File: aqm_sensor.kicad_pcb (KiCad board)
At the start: 2 copper layers, 45 x 30 mm, 14 parts, among them J2 QWIIC, J3 PMS5003, U3 ESP32-C3_SUPERMINI_TH

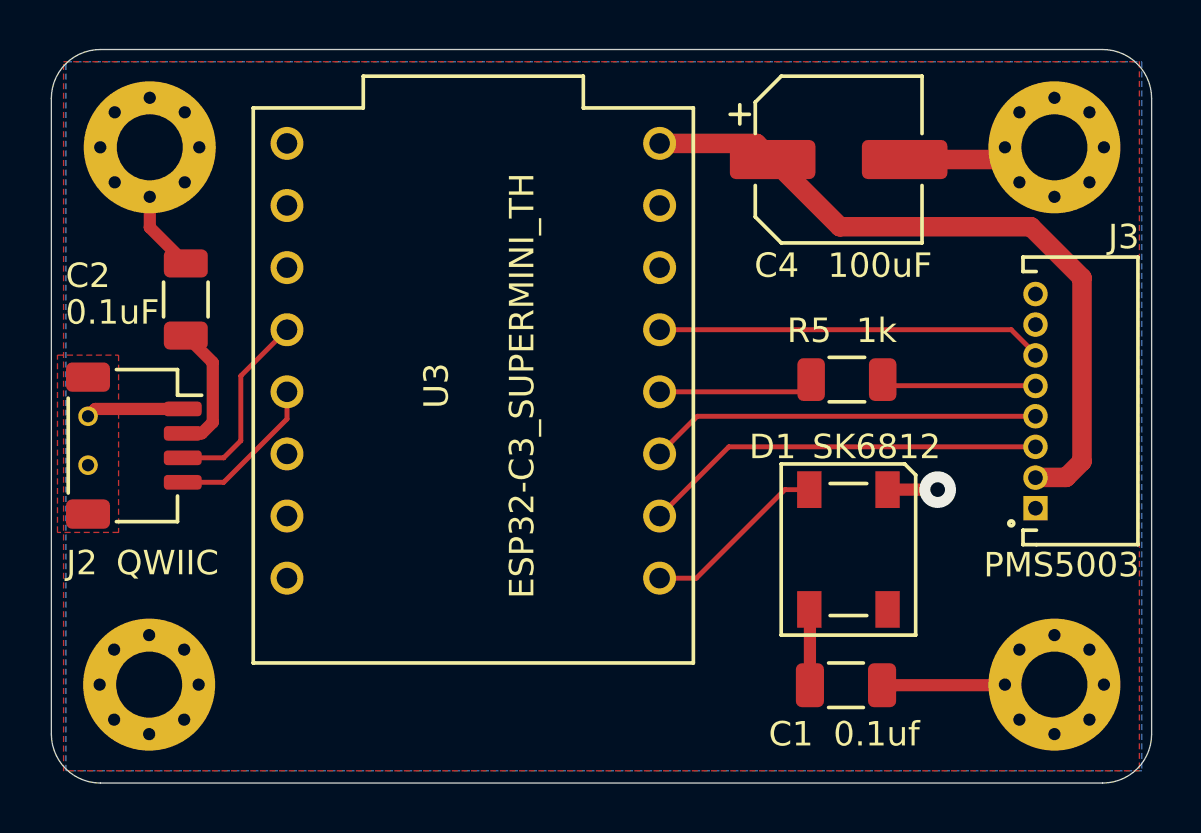
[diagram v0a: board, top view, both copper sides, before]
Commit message: v2 schematic and PCB rework
Schematic:
- Rewire J3 for PMS5003 cable mirror (pin 1↔8 reversal)
- Add I2C pull-up resistors R1, R2 (4.7k) on SDA/SCL
- Replace C4 100uF electrolytic with 10uF 0805 ceramic
- Fix J3 pin types from Unspecified to Passive (ERC clean)
- Add test points: TP1/TP2 (loop) for RX/TX, TP3-TP5 (pad) for power
- Fix C1 value capitalization (0.1uf → 0.1uF)

PCB:
- Rotate U3 180° to correct antenna orientation
- Place new components (R1, R2, C4, TP1-TP5)
- Reroute for updated netlist
- Add GND stitching vias

Removes TODO.md (tracked in CLAUDE.md known issues).

Co-Authored-By: Claude Opus 4.6 (1M context) <noreply@anthropic.com>
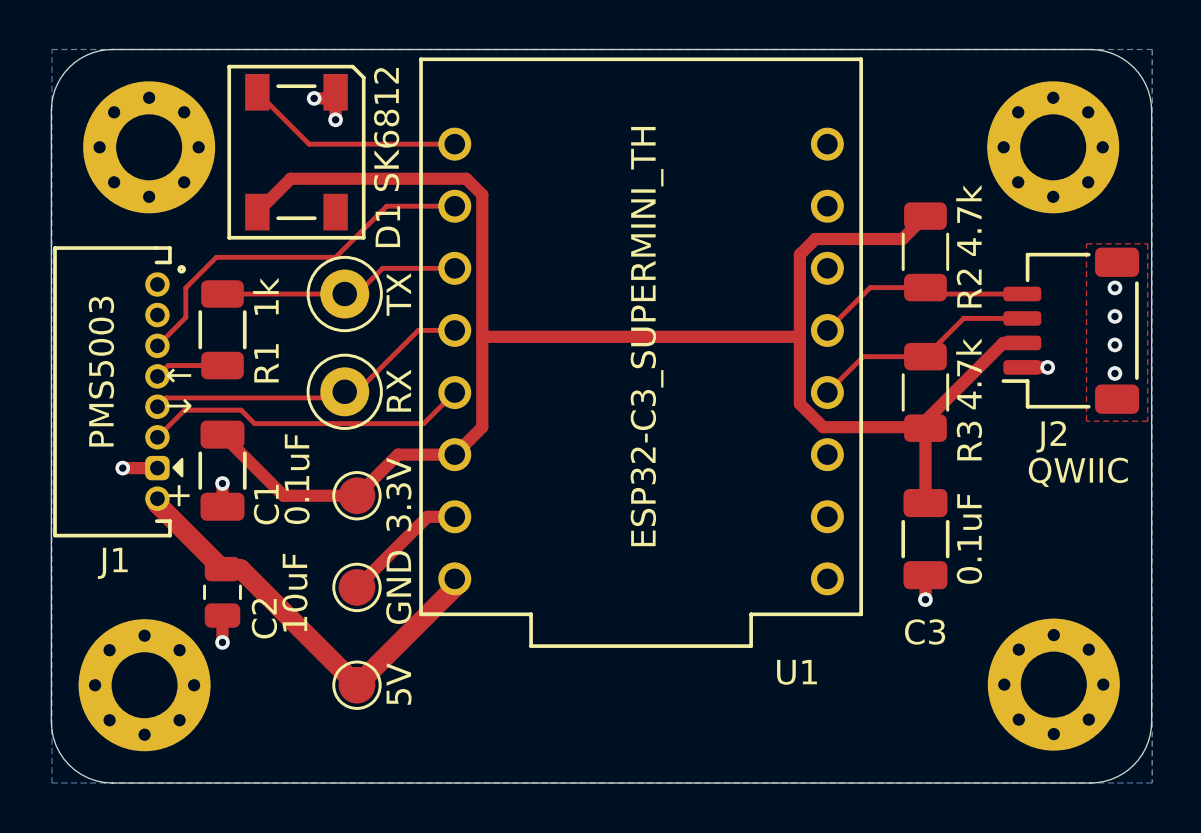
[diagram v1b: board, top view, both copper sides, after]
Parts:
- removed ? (x2): , 
- added R2: 4.7k, Resistor_SMD:R_1206_3216Metric, F.Cu at (181.3, 78.9)
- added R3: 4.7k, Resistor_SMD:R_1206_3216Metric, F.Cu at (181.3, 84.6)
- added TP1: TX, TestPoint:TestPoint_Loop_D2.50mm_Drill1.0mm, F.Cu at (157.6, 80.6)
- added TP2: 3.3V, TestPoint:TestPoint_Pad_D1.5mm, F.Cu at (158.1, 88.8)
- added TP3: RX, TestPoint:TestPoint_Loop_D2.50mm_Drill1.0mm, F.Cu at (157.6, 84.6)
- added TP4: GND, TestPoint:TestPoint_Pad_D1.5mm, F.Cu at (158.1, 92.6)
- added TP5: 5V, TestPoint:TestPoint_Pad_D1.5mm, F.Cu at (158.1, 96.6)
- C1: value 0.1uf -> 0.1uF
- C2: renamed from C4; value 100uF -> 10uF; footprint Capacitor_SMD:CP_Elec_6.3x7.7 -> Capacitor_SMD:C_0805_2012Metric
- moved J2 38.6 mm to (187.3, 82.1), turned to 90 degrees
- moved J1 35.9 mm to (149.9, 84.6), turned to -90 degrees
- moved C3 31.8 mm to (181.3, 90.6), turned to 90 degrees
- moved C2 30.8 mm to (152.6, 92.8), turned to -90 degrees
- moved D1 27.8 mm to (155.6, 74.8)
- moved C1 27.0 mm to (152.6, 87.8), turned to 90 degrees
- moved R1 25.6 mm to (152.6, 82.0), turned to -90 degrees
- moved U1 7.15 mm to (169.7, 82.3), turned to 180 degrees
- moved H2 0.19 mm to (149.4, 96.6)
- renumbered C2 to C3, H3 to H2, H2 to H3, J3 to J1, R5 to R1, U3 to U1
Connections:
- J1 pad 1: GND -> unconnected-(J3-Pad1)
- J1 pad 2: +5V -> unconnected-(J3-Pad2)
- J1 pad 3: /PMS_SET -> /PMS_RESET
- J1 pad 4: /PMS_RX -> Net-(J3-Pad4)
- J1 pad 5: Net-(J3-Pad5) -> /PMS_RX
- J1 pad 6: /PMS_RESET -> /PMS_SET
- J1 pad 7: unconnected-(J3-Pad7) -> GND
- J1 pad 8: unconnected-(J3-Pad8) -> +5V
- R1 pad 2: Net-(J3-Pad5) -> Net-(J3-Pad4)
- U1 pad 1: /PMS_SET -> /PMS_RESET
- U1 pad 2: /PMS_RX -> /PMS_TX
- U1 pad 3: /PMS_TX -> /PMS_RX
- U1 pad 4: /PMS_RESET -> /PMS_SET
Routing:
- net +3.3V: track 8.49 -> 71.1 mm
- net +5V: track 29.2 -> 17.5 mm
- net Net-(J3-Pad5): track 6.05 -> 0.00 mm
- net GND: track 18.0 -> 12.5 mm, vias 1 -> 11
- net /PMS_TX: track 6.40 -> 9.93 mm
- net /PMS_SET: track 16.6 -> 13.4 mm
- net /PMS_RX: track 16.1 -> 13.1 mm
- net Net-(J3-Pad4): track 0.00 -> 2.84 mm
- net /I2C_SCL: track 6.45 -> 8.44 mm
- net /LED: track 7.62 -> 8.95 mm
- net /I2C_SDA: track 7.99 -> 9.23 mm
- net /PMS_RESET: track 15.9 -> 15.2 mm
- removed copper zone on F.Cu, net +3.3V
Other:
- outline, holes or cut-outs redrawn
- board text added: "+"
- board text added: "cehbz aqm_sensor v0.2"
- board text added: "←"
- board text added: "→"
